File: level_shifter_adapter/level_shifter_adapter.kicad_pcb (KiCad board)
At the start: 2 copper layers, 35.6 x 30.5 mm, 45 parts, among them J1 Conn_01x12, J2 Conn_01x12, Q1 BC847, Q2 IRLML6401, Q3 BC847, Q4 IRLML6401, Q5 BC847, U1 GTL2003, U2 MCP1703A-1802_SOT223, U3 ATTINY45-20SU

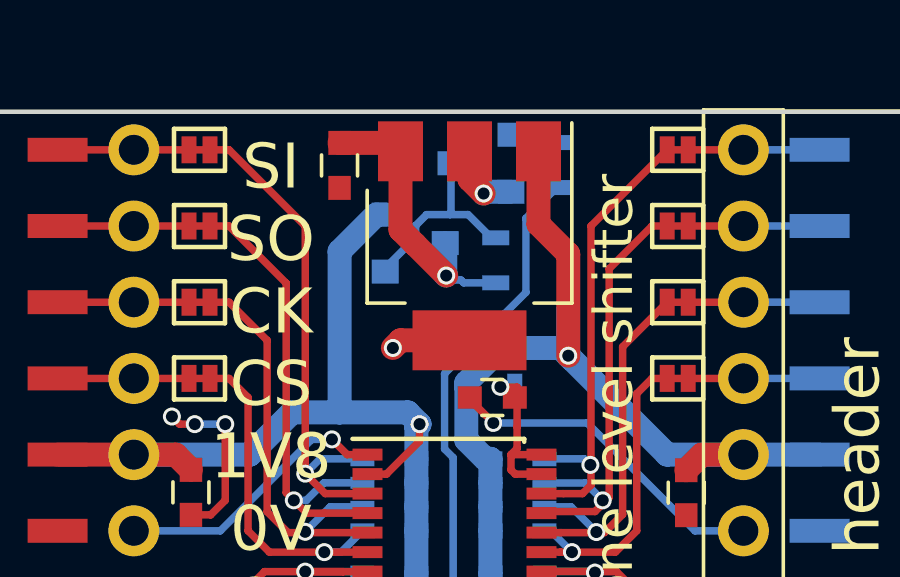
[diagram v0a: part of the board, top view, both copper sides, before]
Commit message: Level shifter finished and fixed - swapping the MCP for 1117
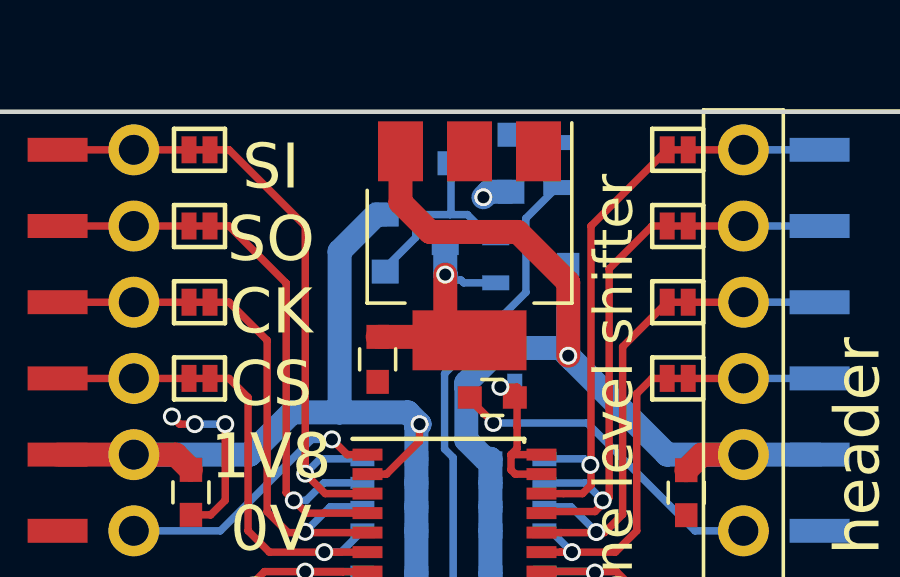
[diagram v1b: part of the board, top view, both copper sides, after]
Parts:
- U2: value MCP1703A-1802_SOT223 -> AP1117-18
- moved C6 6.59 mm to (140.2, 113.7)
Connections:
- U2 pad 1: HVCC -> GND
- U2 pad 2: GND -> +1V8
- U2 pad 3: +1V8 -> HVCC
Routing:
- net GND: track 33.1 -> 28.4 mm, vias 8 -> 7
- net HVCC: track 58.8 -> 62.8 mm
- net +1V8: track 9.77 -> 8.96 mm
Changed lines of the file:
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@@
   (general
     (links 161)
-    (no_connects 0)
+    (no_connects 1)
     (area 124.384999 105.334999 160.095001 135.965001)
     (thickness 1.6)
     (drawings 24)
-    (tracks 475)
+    (tracks 473)
     (zones 0)
     (modules 45)
@@
   )
   (setup
-    (last_trace_width 0.25)
+    (last_trace_width 0.8)
     (user_trace_width 0.4)
     (user_trace_width 0.5)
@@
       (effects (font (size 1 1) (thickness 0.15)))
     )
-    (fp_text value MCP1703A-1802_SOT223 (at 0 4.5 270) (layer F.Fab)
+    (fp_text value AP1117-18 (at 0 4.5 270) (layer F.Fab)
       (effects (font (size 1 1) (thickness 0.15)))
     )
@@
     (fp_line (start 1.85 -3.35) (end 1.85 3.35) (layer F.Fab) (width 0.1))
     (pad 2 smd rect (at 3.15 0 270) (size 2 3.8) (layers F.Cu F.Paste F.Mask)
+      (net 27 +1V8))
+    (pad 2 smd rect (at -3.15 0 270) (size 2 1.5) (layers F.Cu F.Paste F.Mask)
+      (net 27 +1V8))
+    (pad 3 smd rect (at -3.15 2.3 270) (size 2 1.5) (layers F.Cu F.Paste F.Mask)
+      (net 17 HVCC))
+    (pad 1 smd rect (at -3.15 -2.3 270) (size 2 1.5) (layers F.Cu F.Paste F.Mask)
       (net 1 GND))
-    (pad 2 smd rect (at -3.15 0 270) (size 2 1.5) (layers F.Cu F.Paste F.Mask)
-      (net 1 GND))
-    (pad 3 smd rect (at -3.15 2.3 270) (size 2 1.5) (layers F.Cu F.Paste F.Mask)
-      (net 27 +1V8))
-    (pad 1 smd rect (at -3.15 -2.3 270) (size 2 1.5) (layers F.Cu F.Paste F.Mask)
-      (net 17 HVCC))
     (model ${KISYS3DMOD}/TO_SOT_Packages_SMD.3dshapes/SOT-223.wrl
       (at (xyz 0 0 0))
@@
   )
   (module Capacitors_SMD:C_0603 (layer F.Cu)
-    (at 138.938 107.2 270)
+    (at 140.208 113.665 270)
     (descr "Capacitor SMD 0603, reflow soldering, AVX (see smccp.pdf)")
     (tags "capacitor 0603")
@@
     (effects (font (size 1.2 1.2) (thickness 0.25)))
   )
+  (segment (start 143.917793 108.077) (end 143.73278 108.262013) (width 0.8) (layer B.Cu) (net 1))
+  (segment (start 144.653 108.077) (end 143.917793 108.077) (width 0.8) (layer B.Cu) (net 1))
+  (via (at 143.73278 108.262013) (size 0.6) (drill 0.4) (layers F.Cu B.Cu) (net 1))
   (segment (start 145.6436 126.253566) (end 145.963708 125.933458) (width 0.25) (layer B.Cu) (net 1))
   (segment (start 145.6436 126.868) (end 145.6436 126.253566) (width 0.25) (layer B.Cu) (net 1))
   (via (at 145.963708 125.933458) (size 0.6) (drill 0.4) (layers F.Cu B.Cu) (net 1))
-  (segment (start 143.27 106.73) (end 143.27 107.666511) (width 0.8) (layer F.Cu) (net 1))
-  (segment (start 143.27 107.666511) (end 143.740368 108.136879) (width 0.8) (layer F.Cu) (net 1))
   (segment (start 135.128 118.364) (end 135.128 115.824) (width 0.25) (layer F.Cu) (net 1))
   (segment (start 133.985 118.848) (end 134.644 118.848) (width 0.25) (layer F.Cu) (net 1))
   (segment (start 134.644 118.848) (end 135.128 118.364) (width 0.25) (layer F.Cu) (net 1))
-  (segment (start 143.75 113.03) (end 140.97 113.03) (width 0.8) (layer F.Cu) (net 1))
-  (segment (start 140.97 113.03) (end 140.716 113.284) (width 0.8) (layer F.Cu) (net 1))
-  (via (at 140.716 113.284) (size 0.6) (drill 0.4) (layers F.Cu B.Cu) (net 1))
-  (segment (start 144.653 108.077) (end 143.800247 108.077) (width 0.8) (layer B.Cu) (net 1))
-  (segment (start 143.800247 108.077) (end 143.740368 108.136879) (width 0.8) (layer B.Cu) (net 1))
-  (via (at 143.740368 108.136879) (size 0.6) (drill 0.4) (layers F.Cu B.Cu) (net 1))
   (segment (start 143.3562 115.076465) (end 144.06421 115.784475) (width 0.25) (layer F.Cu) (net 1))
   (segment (start 147.191575 115.784475) (end 144.06421 115.784475) (width 0.25) (layer B.Cu) (net 1))
@@
   (segment (start 148.844 119.38) (end 148.844 114.808) (width 0.25) (layer F.Cu) (net 16))
   (segment (start 148.134 120.09) (end 148.844 119.38) (width 0.25) (layer F.Cu) (net 16))
+  (segment (start 146.562099 113.542099) (end 146.562099 111.099681) (width 0.8) (layer F.Cu) (net 17))
+  (segment (start 146.562099 111.099681) (end 144.880522 109.418104) (width 0.8) (layer F.Cu) (net 17))
+  (segment (start 144.880522 109.418104) (end 141.955614 109.418104) (width 0.8) (layer F.Cu) (net 17))
+  (segment (start 141.955614 109.418104) (end 140.97 108.43249) (width 0.8) (layer F.Cu) (net 17))
+  (segment (start 140.97 108.43249) (end 140.97 106.73) (width 0.8) (layer F.Cu) (net 17))
   (segment (start 143.963047 122.801738) (end 143.963047 122.395853) (width 0.25) (layer B.Cu) (net 17))
   (segment (start 143.963047 122.395853) (end 143.9689 122.39) (width 0.25) (layer B.Cu) (net 17))
@@
   (segment (start 143.9689 124.0045) (end 143.9689 123.19) (width 0.7) (layer B.Cu) (net 17))
   (segment (start 144.1704 128.6764) (end 144.1704 127.1016) (width 0.7) (layer B.Cu) (net 17))
-  (segment (start 145.57 106.73) (end 145.57 109.162023) (width 0.8) (layer F.Cu) (net 17))
-  (segment (start 145.57 109.162023) (end 146.562099 110.154122) (width 0.8) (layer F.Cu) (net 17))
-  (segment (start 146.562099 110.154122) (end 146.562099 113.542099) (width 0.8) (layer F.Cu) (net 17))
   (segment (start 146.558 112.014) (end 146.558 113.538) (width 0.8) (layer B.Cu) (net 17))
   (segment (start 146.558 113.538) (end 146.562099 113.542099) (width 0.8) (layer B.Cu) (net 17))
@@
   (segment (start 152.4 116.84) (end 151.015 116.84) (width 0.8) (layer F.Cu) (net 17))
   (segment (start 149.86 116.84) (end 152.4 116.84) (width 0.8) (layer B.Cu) (net 17))
+  (segment (start 140.69 106.45) (end 140.97 106.73) (width 0.8) (layer F.Cu) (net 17))
   (segment (start 147.412204 120.732761) (end 147.45154 120.772097) (width 0.25) (layer B.Cu) (net 18))
   (segment (start 145.826139 120.732761) (end 147.412204 120.732761) (width 0.25) (layer B.Cu) (net 18))
@@
   (segment (start 146.177 106.438) (end 144.914 106.438) (width 0.25) (layer B.Cu) (net 25))
   (segment (start 144.914 106.438) (end 144.653 106.177) (width 0.25) (layer B.Cu) (net 25))
+  (segment (start 143.200368 108.839) (end 143.974368 109.613) (width 0.25) (layer B.Cu) (net 26))
+  (segment (start 143.974368 109.613) (end 144.145 109.613) (width 0.25) (layer B.Cu) (net 26))
+  (segment (start 142.621 108.839) (end 143.200368 108.839) (width 0.25) (layer B.Cu) (net 26))
   (segment (start 141.840786 108.839) (end 142.621 108.839) (width 0.25) (layer B.Cu) (net 26))
-  (segment (start 142.621 108.839) (end 143.223631 108.839) (width 0.25) (layer B.Cu) (net 26))
   (segment (start 142.653 107.127) (end 142.653 108.807) (width 0.25) (layer B.Cu) (net 26))
   (segment (start 142.653 108.807) (end 142.621 108.839) (width 0.25) (layer B.Cu) (net 26))
@@
   (segment (start 141.478 109.601) (end 141.478 109.201786) (width 0.25) (layer B.Cu) (net 26))
   (segment (start 141.478 109.201786) (end 141.840786 108.839) (width 0.25) (layer B.Cu) (net 26))
-  (segment (start 143.223631 108.839) (end 143.997631 109.613) (width 0.25) (layer B.Cu) (net 26))
-  (segment (start 143.997631 109.613) (end 144.145 109.613) (width 0.25) (layer B.Cu) (net 26))
-  (segment (start 138.938 106.45) (end 140.69 106.45) (width 0.8) (layer F.Cu) (net 27))
-  (segment (start 140.69 106.45) (end 140.97 106.73) (width 0.8) (layer F.Cu) (net 27))
-  (segment (start 140.97 106.73) (end 140.97 109.347) (width 0.8) (layer F.Cu) (net 27))
-  (segment (start 140.97 109.347) (end 141.45 109.827) (width 0.8) (layer F.Cu) (net 27))
-  (segment (start 141.45 109.827) (end 142.494 110.871) (width 0.8) (layer F.Cu) (net 27))
+  (segment (start 143.75 113.03) (end 142.276676 113.03) (width 0.8) (layer F.Cu) (net 27))
+  (segment (start 142.276676 113.03) (end 142.161676 112.915) (width 0.8) (layer F.Cu) (net 27))
+  (segment (start 142.161676 112.915) (end 140.208 112.915) (width 0.8) (layer F.Cu) (net 27))
+  (segment (start 142.462 110.839) (end 142.462 112.222) (width 0.8) (layer F.Cu) (net 27))
+  (segment (start 142.462 112.222) (end 143.27 113.03) (width 0.8) (layer F.Cu) (net 27))
+  (via (at 142.462 110.839) (size 0.6) (drill 0.4) (layers F.Cu B.Cu) (net 27))
   (segment (start 144.145 111.113) (end 143.077959 111.113) (width 0.25) (layer B.Cu) (net 27))
   (segment (start 143.077959 111.113) (end 142.985764 111.020805) (width 0.25) (layer B.Cu) (net 27))
@@
   (segment (start 142.462 109.789) (end 142.462 110.839) (width 0.8) (layer B.Cu) (net 27))
   (segment (start 142.462 110.839) (end 142.494 110.871) (width 0.8) (layer B.Cu) (net 27))
-  (via (at 142.494 110.871) (size 0.6) (drill 0.4) (layers F.Cu B.Cu) (net 27))
   (segment (start 146.9644 125.984) (end 146.9644 126.5428) (width 0.25) (layer B.Cu) (net 28))
   (segment (start 146.9644 126.5428) (end 147.066 126.6444) (width 0.25) (layer B.Cu) (net 28))
